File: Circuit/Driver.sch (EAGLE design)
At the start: 33 parts

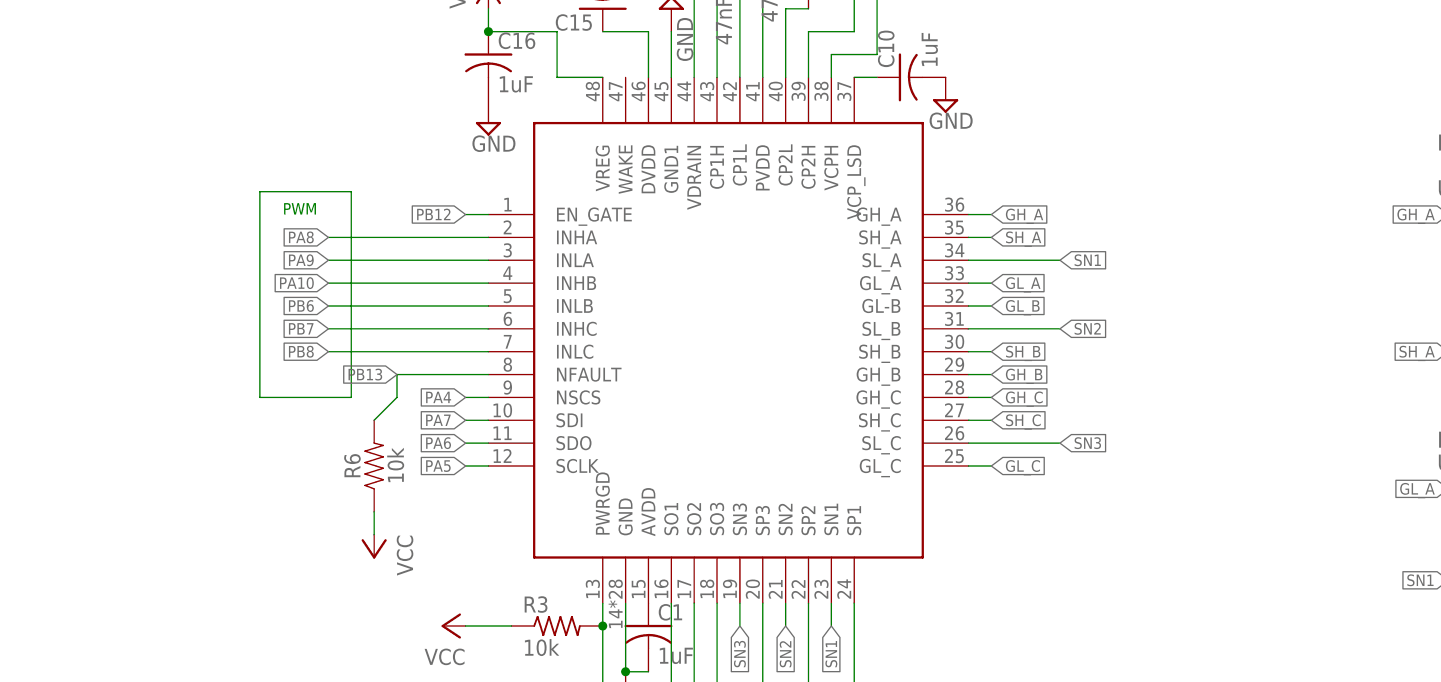
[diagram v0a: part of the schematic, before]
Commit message: enlarged the width of the vin and added a T-stop wire for large current signal (mosfet GND and VCC)
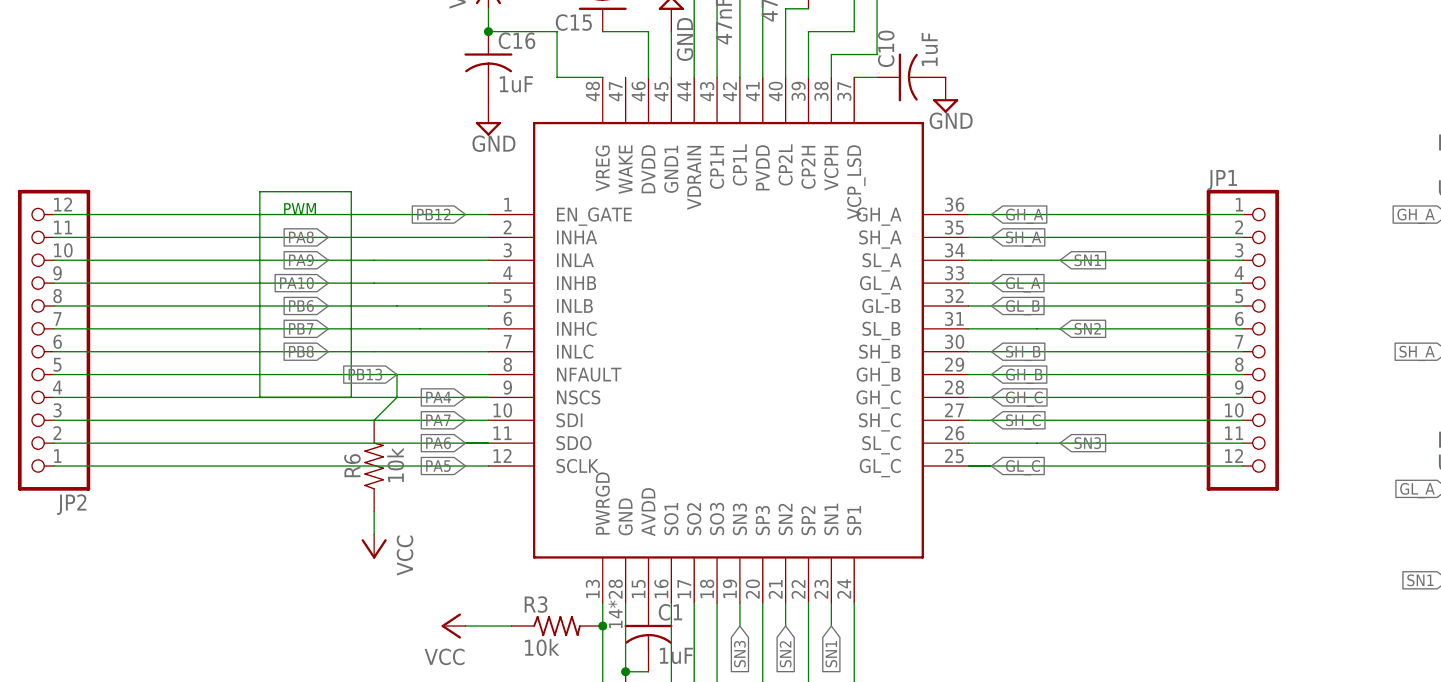
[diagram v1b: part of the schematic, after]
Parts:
- added JP1, JP2: (no value), pinhead:PINHD-1X12
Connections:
- net GH_A: now also JP1.1
- net GH_B: now also JP1.8
- net GH_C: now also JP1.9
- net GL_A: now also JP1.4
- net GL_B: now also JP1.5
- net GL_C: now also JP1.12
- net PA10: now also JP2.9
- net PA4: now also JP2.4
- net PA5: now also JP2.1
- net PA6: now also JP2.2
- net PA7: now also JP2.3
- net PA8: now also JP2.11
- net PA9: now also JP2.10
- net PB12: now also JP2.12
- net PB13: now also JP2.5
- net PB6: now also JP2.8
- net PB7: now also JP2.7
- net PB8: now also JP2.6
- net SH_A: now also JP1.2
- net SH_B: now also JP1.7
- net SH_C: now also JP1.10
- net SN1: now also JP1.3
- net SN2: now also JP1.6
- net SN3: now also JP1.11

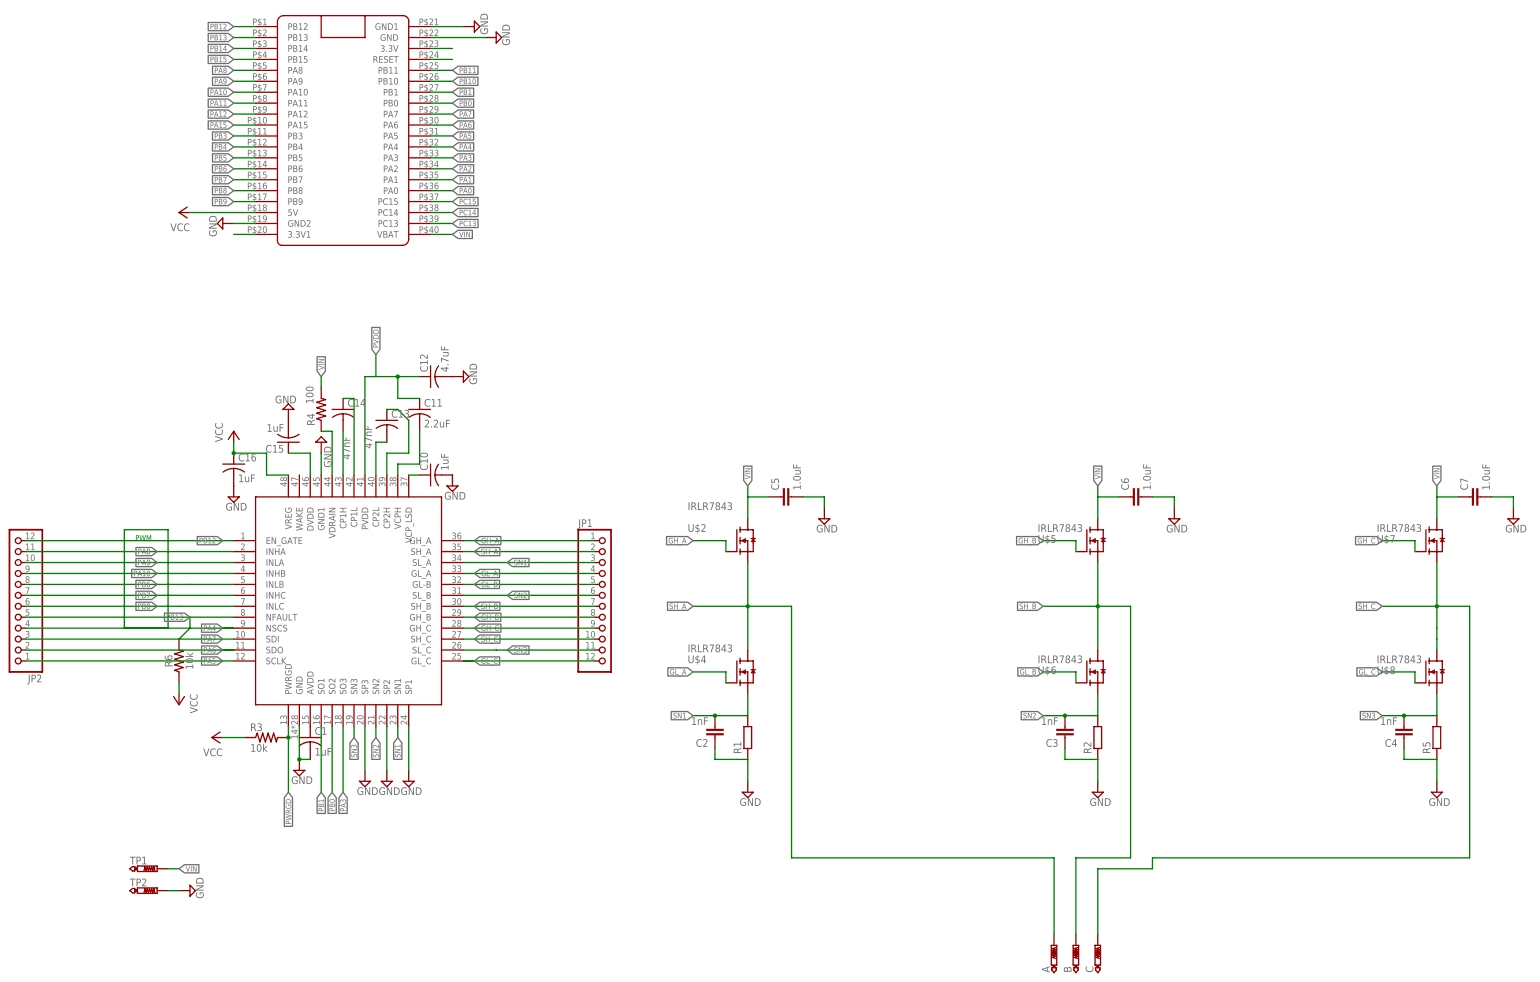
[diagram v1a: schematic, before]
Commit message: fixed some bugs(Erc and Drc Errors)
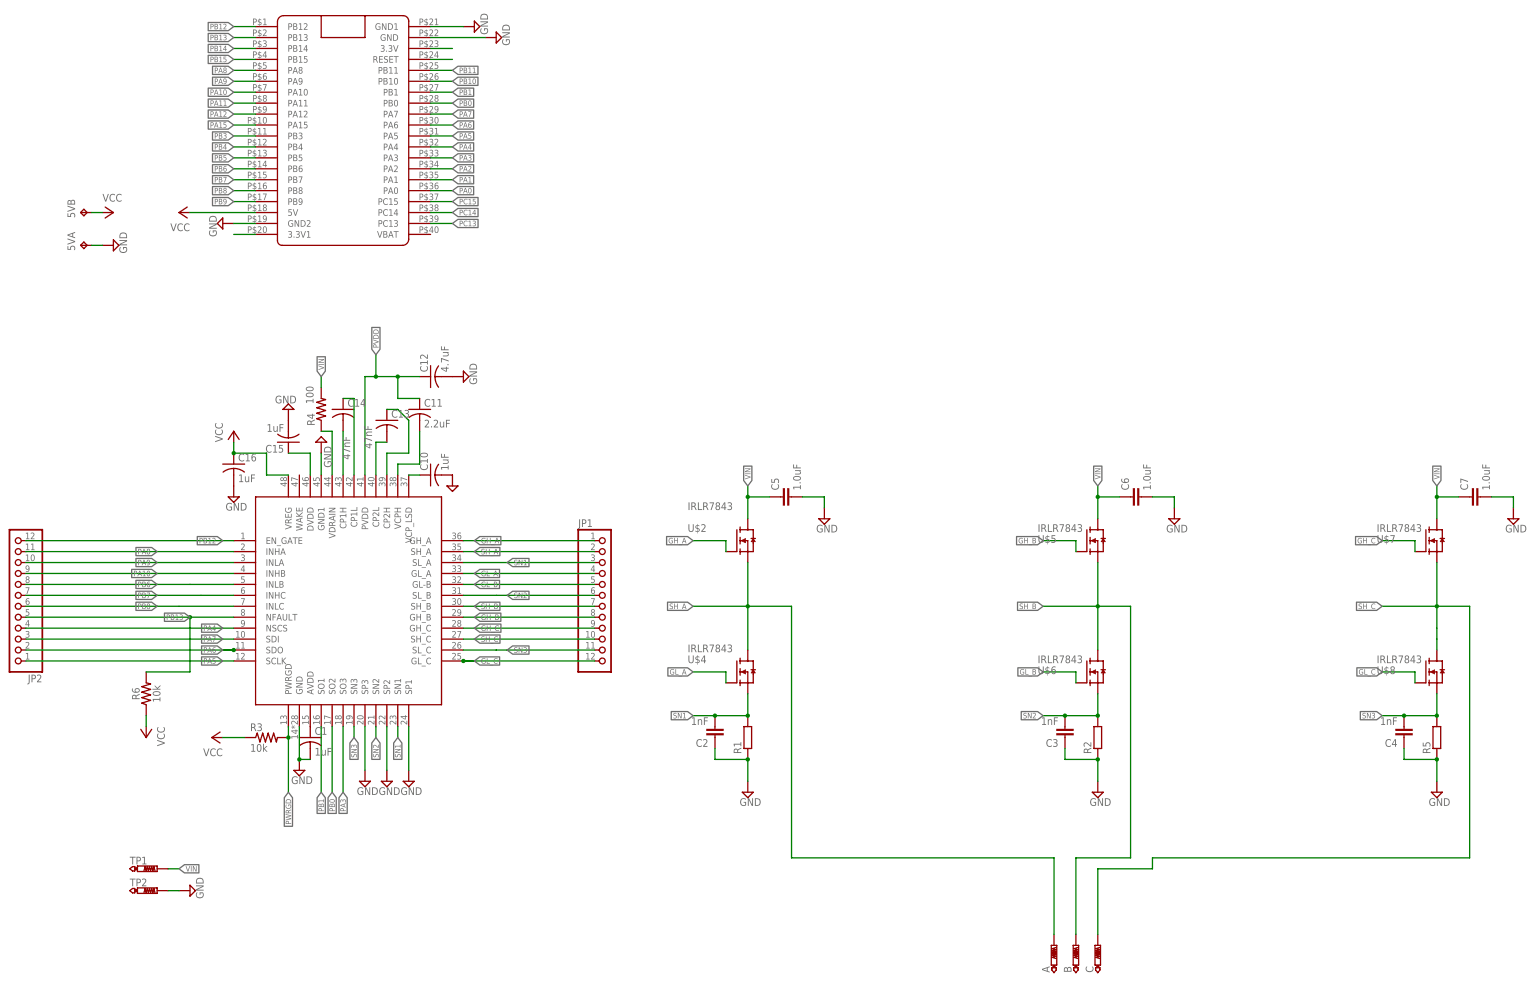
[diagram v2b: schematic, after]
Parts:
- added 5V: TP2P2-38-17, testpad:TP2P2-38-17
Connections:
- removed net VIN1: C6.1
- removed net VIN2: C7.1
- removed net VREG: C16.1, U$3.VREG
- net GND: now also 5VA.TP
- net VCC: now also 5VB.TP, C16.1, U$3.VREG
- net VIN: now also C6.1, C7.1; no longer U$1.VBAT
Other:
- note removed: "PWM"
- moved on the sheet: R6

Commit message: Fixed the PVDD and VDrain pin's 'Vin' problem, Fixed some bugs
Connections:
- removed net PVDD: C11.1, C12.1, U$3.PVDD
- net VIN: now also C11.1, C12.1, U$3.PVDD
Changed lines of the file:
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@@
 <pinref part="TP1" gate="G$1" pin="TP"/>
+</segment>
+<segment>
+<pinref part="C11" gate="G$1" pin="1"/>
+<wire x1="63.5" y1="48.26" x2="66.04" y2="48.26" width="0.1524" layer="91"/>
+<wire x1="66.04" y1="48.26" x2="71.12" y2="48.26" width="0.1524" layer="91"/>
+<wire x1="71.12" y1="48.26" x2="71.12" y2="43.18" width="0.1524" layer="91"/>
+<wire x1="71.12" y1="43.18" x2="76.2" y2="43.18" width="0.1524" layer="91"/>
+<pinref part="U$3" gate="G$1" pin="PVDD"/>
+<wire x1="63.5" y1="25.4" x2="63.5" y2="48.26" width="0.1524" layer="91"/>
+<pinref part="C12" gate="G$1" pin="1"/>
+<wire x1="76.2" y1="48.26" x2="71.12" y2="48.26" width="0.1524" layer="91"/>
+<junction x="71.12" y="48.26"/>
+<wire x1="66.04" y1="48.26" x2="66.04" y2="53.34" width="0.1524" layer="91"/>
+<label x="66.04" y="53.34" size="1.27" layer="95" rot="R90" xref="yes"/>
+<junction x="66.04" y="48.26"/>
 </segment>
 </net>
@@
 </segment>
 </net>
-<net name="PVDD" class="0">
-<segment>
-<pinref part="C11" gate="G$1" pin="1"/>
-<wire x1="63.5" y1="48.26" x2="66.04" y2="48.26" width="0.1524" layer="91"/>
-<wire x1="66.04" y1="48.26" x2="71.12" y2="48.26" width="0.1524" layer="91"/>
-<wire x1="71.12" y1="48.26" x2="71.12" y2="43.18" width="0.1524" layer="91"/>
-<wire x1="71.12" y1="43.18" x2="76.2" y2="43.18" width="0.1524" layer="91"/>
-<pinref part="U$3" gate="G$1" pin="PVDD"/>
-<wire x1="63.5" y1="25.4" x2="63.5" y2="48.26" width="0.1524" layer="91"/>
-<pinref part="C12" gate="G$1" pin="1"/>
-<wire x1="76.2" y1="48.26" x2="71.12" y2="48.26" width="0.1524" layer="91"/>
-<junction x="71.12" y="48.26"/>
-<wire x1="66.04" y1="48.26" x2="66.04" y2="53.34" width="0.1524" layer="91"/>
-<label x="66.04" y="53.34" size="1.27" layer="95" rot="R90" xref="yes"/>
-<junction x="66.04" y="48.26"/>
-</segment>
-</net>
